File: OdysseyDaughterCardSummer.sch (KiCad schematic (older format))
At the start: 26 parts, among them J1 Conn_01x01, J2 Conn_01x01, J3 Conn_01x01, J4 Conn_01x01, X1 OdysseyDaughterCard

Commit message: R1.0 remove extra player hardware and replace with single port
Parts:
- removed D10, D9: 1N4448, Diode_THT:D_DO-35_SOD27_P7.62mm_Horizontal, symbol Device:D
- removed D11, D12: BAT83S, Diode_THT:D_DO-35_SOD27_P7.62mm_Horizontal, symbol Device:D_Schottky
- removed J1, J2, J3, J4: Conn_01x01, Connector_Wire:SolderWirePad_single_1-5mmDrill, symbol Connector_Generic:Conn_01x01
- removed R8, R9: 0, Resistor_THT:R_Axial_DIN0207_L6.3mm_D2.5mm_P7.62mm_Horizontal, symbol Device:R
- added J1: Conn_01x02, Connector_PinHeader_2.54mm:PinHeader_1x02_P2.54mm_Vertical, symbol Connector_Generic:Conn_01x02
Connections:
- wire segments 63 -> 50
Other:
- note added: "Ball Signal Out"
- note added: "Extra Players In"
- note removed: "Extra player inputs"
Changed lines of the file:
@@
 Sheet 1 1
 Title "Odyssey Daughter Card Summer"
-Date "2018-08-18"
-Rev "0.1"
+Date "2018-11-23"
+Rev "1.0"
 Comp "University of Pittsburgh - Odyssey Restoration Project"
 Comment1 "Levi Burner"
@@
 Card10
 $Comp
-L Device:D D10
-U 1 1 5B790856
-P 5750 3200
-F 0 "D10" H 5750 2984 50  0000 C CNN
-F 1 "1N4448" H 5750 3075 50  0000 C CNN
-F 2 "Diode_THT:D_DO-35_SOD27_P7.62mm_Horizontal" H 5750 3200 50  0001 C CNN
-F 3 "~" H 5750 3200 50  0001 C CNN
-	1    5750 3200
-	-1   0    0    1
-$EndComp
-$Comp
-L Device:D D9
-U 1 1 5B790898
-P 5750 2500
-F 0 "D9" H 5750 2284 50  0000 C CNN
-F 1 "1N4448" H 5750 2375 50  0000 C CNN
-F 2 "Diode_THT:D_DO-35_SOD27_P7.62mm_Horizontal" H 5750 2500 50  0001 C CNN
-F 3 "~" H 5750 2500 50  0001 C CNN
-	1    5750 2500
-	-1   0    0    1
-$EndComp
-Wire Wire Line
-	5900 3200 6000 3200
-Wire Wire Line
-	6000 3200 6000 3750
-Wire Wire Line
-	5900 2500 6000 2500
-Wire Wire Line
-	6000 2500 6000 3200
-Connection ~ 6000 3200
-Wire Wire Line
-	5600 2500 5550 2500
-Wire Wire Line
-	5600 3200 5550 3200
-$Comp
-L Connector_Generic:Conn_01x01 J3
-U 1 1 5B7939F4
-P 4550 3200
-F 0 "J3" H 4470 2975 50  0000 C CNN
-F 1 "Conn_01x01" H 4470 3066 50  0000 C CNN
-F 2 "Connector_Wire:SolderWirePad_single_1-5mmDrill" H 4550 3200 50  0001 C CNN
-F 3 "~" H 4550 3200 50  0001 C CNN
-	1    4550 3200
-	-1   0    0    1
-$EndComp
-$Comp
-L Connector_Generic:Conn_01x01 J1
-U 1 1 5B793A6A
-P 4550 2500
-F 0 "J1" H 4470 2275 50  0000 C CNN
-F 1 "Conn_01x01" H 4470 2366 50  0000 C CNN
-F 2 "Connector_Wire:SolderWirePad_single_1-5mmDrill" H 4550 2500 50  0001 C CNN
-F 3 "~" H 4550 2500 50  0001 C CNN
-	1    4550 2500
-	-1   0    0    1
-$EndComp
-$Comp
-L Device:R R8
-U 1 1 5B797289
-P 5400 2500
-F 0 "R8" V 5607 2500 50  0000 C CNN
-F 1 "0" V 5516 2500 50  0000 C CNN
-F 2 "Resistor_THT:R_Axial_DIN0207_L6.3mm_D2.5mm_P7.62mm_Horizontal" V 5330 2500 50  0001 C CNN
-F 3 "~" H 5400 2500 50  0001 C CNN
-	1    5400 2500
-	0    -1   -1   0
-$EndComp
-Wire Wire Line
-	5250 2500 5200 2500
-$Comp
-L Device:R R9
-U 1 1 5B797380
-P 5400 3200
-F 0 "R9" V 5607 3200 50  0000 C CNN
-F 1 "0" V 5516 3200 50  0000 C CNN
-F 2 "Resistor_THT:R_Axial_DIN0207_L6.3mm_D2.5mm_P7.62mm_Horizontal" V 5330 3200 50  0001 C CNN
-F 3 "~" H 5400 3200 50  0001 C CNN
-	1    5400 3200
-	0    -1   -1   0
-$EndComp
-Wire Wire Line
-	5250 3200 5200 3200
-$Comp
 L Device:R R4
 U 1 1 5B7991E8
@@
 	5250 5950 4750 5950
 $Comp
-L Device:D_Schottky D12
-U 1 1 5B7997A7
-P 5000 3550
-F 0 "D12" H 5000 3334 50  0000 C CNN
-F 1 "BAT83S" H 5000 3425 50  0000 C CNN
-F 2 "Diode_THT:D_DO-35_SOD27_P7.62mm_Horizontal" H 5000 3550 50  0001 C CNN
-F 3 "~" H 5000 3550 50  0001 C CNN
-	1    5000 3550
-	-1   0    0    1
-$EndComp
-$Comp
-L Device:D_Schottky D11
-U 1 1 5B79985B
-P 5000 2850
-F 0 "D11" H 5000 2634 50  0000 C CNN
-F 1 "BAT83S" H 5000 2725 50  0000 C CNN
-F 2 "Diode_THT:D_DO-35_SOD27_P7.62mm_Horizontal" H 5000 2850 50  0001 C CNN
-F 3 "~" H 5000 2850 50  0001 C CNN
-	1    5000 2850
-	-1   0    0    1
-$EndComp
-$Comp
-L Connector_Generic:Conn_01x01 J2
-U 1 1 5B79DE19
-P 4550 2850
-F 0 "J2" H 4470 2625 50  0000 C CNN
-F 1 "Conn_01x01" H 4470 2716 50  0000 C CNN
-F 2 "Connector_Wire:SolderWirePad_single_1-5mmDrill" H 4550 2850 50  0001 C CNN
-F 3 "~" H 4550 2850 50  0001 C CNN
-	1    4550 2850
-	-1   0    0    1
-$EndComp
-Wire Wire Line
-	4750 2850 4850 2850
-Wire Wire Line
-	5150 2850 5200 2850
-Wire Wire Line
-	5200 2850 5200 2500
-Connection ~ 5200 2500
-Wire Wire Line
-	5200 2500 4750 2500
-$Comp
-L Connector_Generic:Conn_01x01 J4
-U 1 1 5B7A2B6E
-P 4550 3550
-F 0 "J4" H 4470 3325 50  0000 C CNN
-F 1 "Conn_01x01" H 4470 3416 50  0000 C CNN
-F 2 "Connector_Wire:SolderWirePad_single_1-5mmDrill" H 4550 3550 50  0001 C CNN
-F 3 "~" H 4550 3550 50  0001 C CNN
-	1    4550 3550
-	-1   0    0    1
-$EndComp
-Wire Wire Line
-	5150 3550 5200 3550
-Wire Wire Line
-	5200 3550 5200 3200
-Connection ~ 5200 3200
-Wire Wire Line
-	5200 3200 4750 3200
-Wire Wire Line
-	4750 3550 4850 3550
-Wire Notes Line
-	4300 2200 4300 3650
-Wire Notes Line
-	4300 3650 5250 3650
-Wire Notes Line
-	5250 3650 5250 3400
-Wire Notes Line
-	5250 3400 6100 3400
-Wire Notes Line
-	6100 3400 6100 2200
-Wire Notes Line
-	6100 2200 4300 2200
-Text Notes 4300 2150 0    60   ~ 0
-Extra player inputs
+L Connector_Generic:Conn_01x02 J1
+U 1 1 5BF8D91F
+P 4800 2800
+F 0 "J1" H 4720 3017 50  0000 C CNN
+F 1 "Conn_01x02" H 4720 2926 50  0000 C CNN
+F 2 "Connector_PinHeader_2.54mm:PinHeader_1x02_P2.54mm_Vertical" H 4800 2800 50  0001 C CNN
+F 3 "~" H 4800 2800 50  0001 C CNN
+	1    4800 2800
+	-1   0    0    -1
+$EndComp
+Wire Wire Line
+	5000 2900 5200 2900
+Wire Wire Line
+	6000 2800 6000 3750
+Wire Wire Line
+	5000 2800 6000 2800
+Text Label 5200 2900 0    60   ~ 0
+Card5
+Text Notes 3950 2800 0    60   ~ 0
+Extra Players In
+Text Notes 3950 2900 0    60   ~ 0
+Ball Signal Out
 $EndSCHEMATC

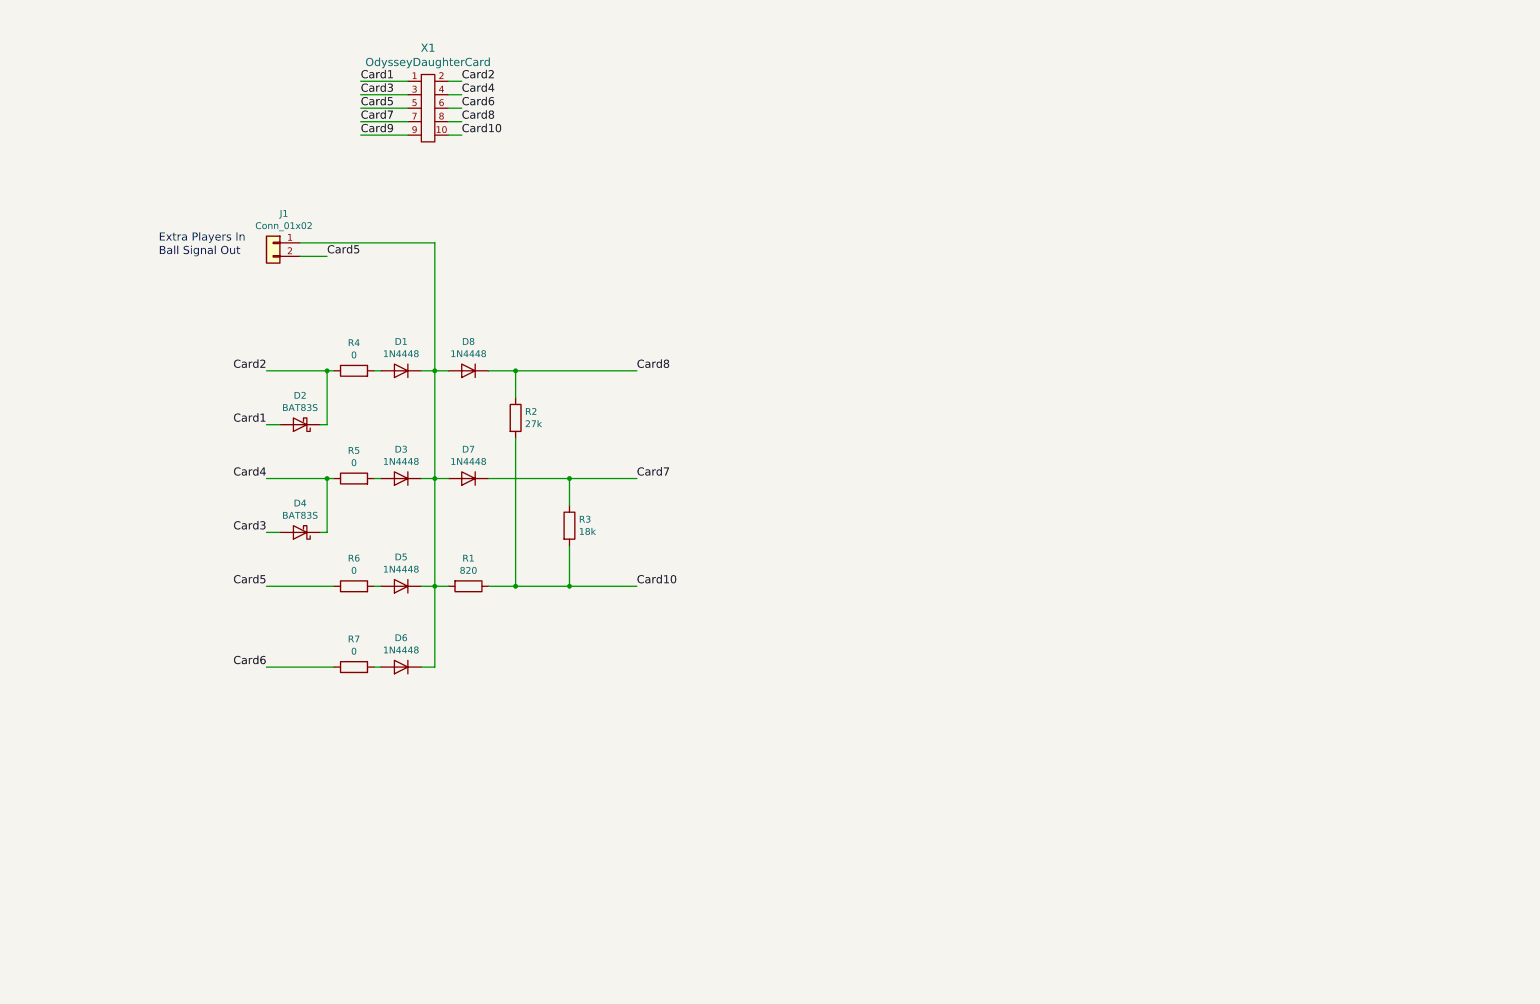
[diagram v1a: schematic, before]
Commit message: R1.1 with video mod pre layout
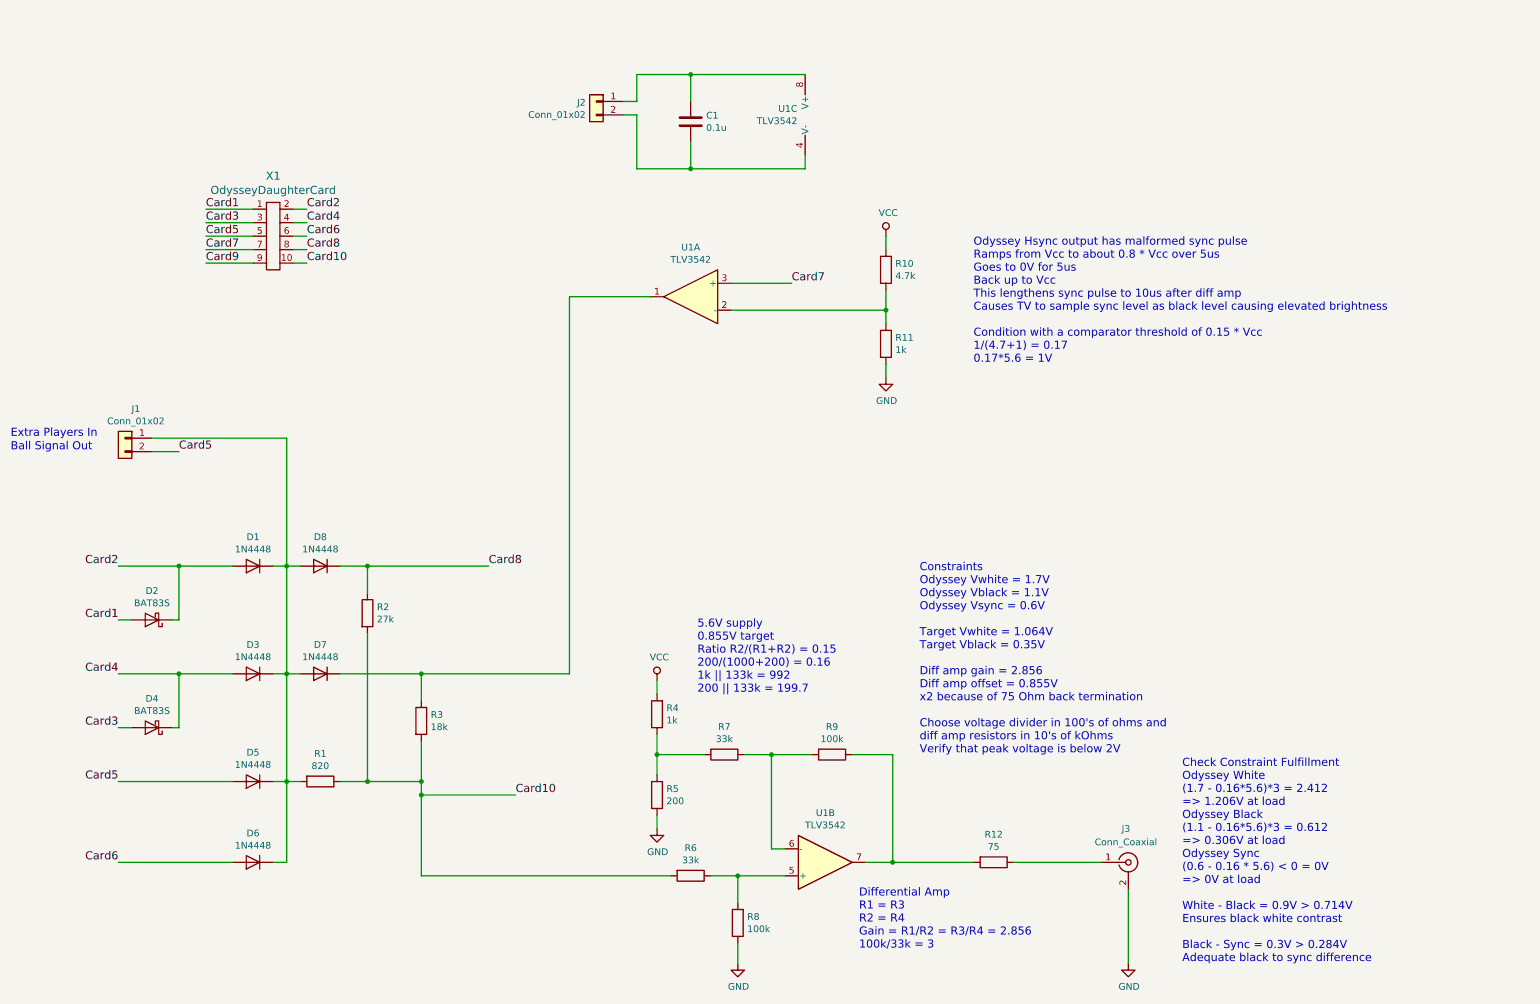
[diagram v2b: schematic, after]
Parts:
- added C1: 0.1u, Capacitor_THT:C_Disc_D3.8mm_W2.6mm_P2.50mm, symbol Device:C
- added J2: Conn_01x02, Connector_PinHeader_2.54mm:PinHeader_1x02_P2.54mm_Vertical, symbol Connector_Generic:Conn_01x02
- added J3: Conn_Coaxial, RCA_Switchcraft_PJRAN1X1U04X:CONN_RCA_JACK_MONO_3.2MM_Switchcraft_PJRAN1X1U04X, symbol Connector:Conn_Coaxial
- added R10: 4.7k, Resistor_THT:R_Axial_DIN0207_L6.3mm_D2.5mm_P7.62mm_Horizontal, symbol Device:R
- added R11: 1k, Resistor_THT:R_Axial_DIN0207_L6.3mm_D2.5mm_P7.62mm_Horizontal, symbol Device:R
- added R12: 75, Resistor_THT:R_Axial_DIN0207_L6.3mm_D2.5mm_P7.62mm_Horizontal, symbol Device:R
- added R8, R9: 100k, Resistor_THT:R_Axial_DIN0207_L6.3mm_D2.5mm_P7.62mm_Horizontal, symbol Device:R
- added U1: TLV3542, Package_SO:SOIC-8_3.9x4.9mm_P1.27mm, symbol TLV3542:TLV3542
- R4: value 0 -> 1k
- R5: value 0 -> 200
- R6, R7: value 0 -> 33k
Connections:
- net Card10: now also R6.2
- net Card2: now also D1.2 (A); no longer R4.1
- net Card4: now also D3.2 (A); no longer R5.1
- net Card5: now also D5.2 (A); no longer R6.1
- net Card6: now also D6.2 (A); no longer R7.1
- net Card7: now also U1.3 (+); no longer D7.1 (K), R3.1
- net VCC: now reaches R4.2
- net VCC: now also R10.1; no longer D1.2 (A)
- net at R5.2: now also R4.1, R7.2; no longer D3.2 (A)
- new net: D7.1 (K), R3.1, U1.1
- new net: R10.2, R11.1, U1.2 (-)
- new net: R6.1, R8.2, U1.5 (+)
- new net: R7.1, R9.2, U1.6 (-)
- new net: R12.2, R9.1, U1.7
- new net: C1.2, J2.2 (Pin_2), U1.4 (V-)
- new net: C1.1, J2.1 (Pin_1), U1.8 (V+)
- new net: J3.1 (In), R12.1
- new net GND: J3.2 (Ext), R11.2, R5.1, R8.1
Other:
- note added: "5.6V supply\n0.855V target\nRatio R2/(R1+R2) = 0.15\n200/(1000+200) = 0.16\n1k || 133k = 992\n200 || 133k = 199.7"
- note added: "Check Constraint Fulfillment\nOdyssey White\n(1.7 - 0.16*5.6)*3 = 2.412 \n=> 1.206V at load\nOdyssey Black\n(1.1 - 0.16*5.6)*3 = 0.612\n=> 0.306V at load\nOdyssey Sync\n(0.6 - 0.16 * 5.6) < 0 = 0V\n=> 0V at load\n\nWhite - Black = 0.9V > 0.714V\nEnsures black white contrast\n\nBlack - Sync = 0.3V > 0.284V\nAdequate black to sync difference"
- note added: "Constraints\nOdyssey Vwhite = 1.7V\nOdyssey Vblack = 1.1V\nOdyssey Vsync = 0.6V\n\nTarget Vwhite = 1.064V\nTarget Vblack = 0.35V\n\nDiff amp gain = 2.856\nDiff amp offset = 0.855V\nx2 because of 75 Ohm back termination\n\nChoose voltage divider in 100's of ohms and\ndiff amp resistors in 10's of kOhms\nVerify that peak voltage is below 2V"
- note added: "Differential Amp\nR1 = R3\nR2 = R4\nGain = R1/R2 = R3/R4 = 2.856\n100k/33k = 3"
- note added: "Odyssey Hsync output has malformed sync pulse\nRamps from Vcc to about 0.8 * Vcc over 5us\nGoes to 0V for 5us\nBack up to Vcc\nThis lengthens sync pulse to 10us after diff amp\nCauses TV to sample sync level as black level causing elevated brightness\n\nCondition with a comparator threshold of 0.15 * Vcc\n1/(4.7+1) = 0.17\n0.17*5.6 = 1V"
- moved on the sheet: D1, D2, D3, D4, D5, D6, D7, D8, J1, R1, R2, R3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

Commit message: R1.1 gerbs and board NTSC generator
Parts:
- J3: footprint RCA_Switchcraft_PJRAN1X1U04X:CONN_RCA_JACK_MONO_3.2MM_Switchcraft_PJRAN1X1U04X -> Connector_PinHeader_2.54mm:PinHeader_1x02_P2.54mm_Vertical
- R4: value 1k -> 4.7k
- R5: value 200 -> 820
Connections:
- net GND: now also C1.2, J2.2 (Pin_2), U1.4 (V-)
- net VCC: now also C1.1, J2.1 (Pin_1), U1.8 (V+)
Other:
- note added: "5.6V supply\n0.855V target\nRatio R2/(R1+R2) = 0.15\n820/(4700+820) = 0.15\n4.7k || 133k = 4.5k\n820 || 133k = 815"
- note added: "Check Constraint Fulfillment\nOdyssey White\n(1.7 - 0.15*5.6)*3 = 2.58 \n=> 1.29V at load\nOdyssey Black\n(1.1 - 0.16*5.6)*3 = 0.780\n=> 0.390V at load\nOdyssey Sync\n(0.6 - 0.15 * 5.6) < 0 = 0V\n=> 0V at load\n\nWhite - Black = 0.9V > 0.714V\nEnsures black white contrast\n\nBlack - Sync = 0.39V > 0.284V\nAdequate black to sync difference"
- note removed: "5.6V supply\n0.855V target\nRatio R2/(R1+R2) = 0.15\n200/(1000+200) = 0.16\n1k || 133k = 992\n200 || 133k = 199.7"
- note removed: "Check Constraint Fulfillment\nOdyssey White\n(1.7 - 0.16*5.6)*3 = 2.412 \n=> 1.206V at load\nOdyssey Black\n(1.1 - 0.16*5.6)*3 = 0.612\n=> 0.306V at load\nOdyssey Sync\n(0.6 - 0.16 * 5.6) < 0 = 0V\n=> 0V at load\n\nWhite - Black = 0.9V > 0.714V\nEnsures black white contrast\n\nBlack - Sync = 0.3V > 0.284V\nAdequate black to sync difference"
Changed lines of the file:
@@
 Wire Wire Line
 	4650 2850 4300 2850
-Wire Wire Line
-	4650 2950 4300 2950
 $Comp
 L Device:D D1
@@
 F 3 "" H 8750 1850 50  0001 C CNN
 	3    8750 1850
-	-1   0    0    -1
+	1    0    0    -1
 $EndComp
 $Comp
@@
 P 7650 6300
 F 0 "R4" H 7580 6254 50  0000 R CNN
-F 1 "1k" H 7580 6345 50  0000 R CNN
+F 1 "4.7k" H 7580 6345 50  0000 R CNN
 F 2 "Resistor_THT:R_Axial_DIN0207_L6.3mm_D2.5mm_P7.62mm_Horizontal" V 7580 6300 50  0001 C CNN
 F 3 "~" H 7650 6300 50  0001 C CNN
@@
 P 7650 6900
 F 0 "R5" H 7580 6854 50  0000 R CNN
-F 1 "200" H 7580 6945 50  0000 R CNN
+F 1 "820" H 7580 6945 50  0000 R CNN
 F 2 "Resistor_THT:R_Axial_DIN0207_L6.3mm_D2.5mm_P7.62mm_Horizontal" V 7580 6900 50  0001 C CNN
 F 3 "~" H 7650 6900 50  0001 C CNN
@@
 Wire Wire Line
 	9400 7400 10000 7400
-$Comp
-L Connector:Conn_Coaxial J3
-U 1 1 5C5FC8A0
-P 11150 7400
-F 0 "J3" H 11100 7650 50  0000 L CNN
-F 1 "Conn_Coaxial" H 10900 7550 50  0000 L CNN
-F 2 "RCA_Switchcraft_PJRAN1X1U04X:CONN_RCA_JACK_MONO_3.2MM_Switchcraft_PJRAN1X1U04X" H 11150 7400 50  0001 C CNN
-F 3 " ~" H 11150 7400 50  0001 C CNN
-	1    11150 7400
-	1    0    0    -1
-$EndComp
 Wire Wire Line
 	10300 7400 10950 7400
@@
 Constraints\nOdyssey Vwhite = 1.7V\nOdyssey Vblack = 1.1V\nOdyssey Vsync = 0.6V\n\nTarget Vwhite = 1.064V\nTarget Vblack = 0.35V\n\nDiff amp gain = 2.856\nDiff amp offset = 0.855V\nx2 because of 75 Ohm back termination\n\nChoose voltage divider in 100's of ohms and\ndiff amp resistors in 10's of kOhms\nVerify that peak voltage is below 2V
 Text Notes 7950 6150 0    60   ~ 0
-5.6V supply\n0.855V target\nRatio R2/(R1+R2) = 0.15\n200/(1000+200) = 0.16\n1k || 133k = 992\n200 || 133k = 199.7
+5.6V supply\n0.855V target\nRatio R2/(R1+R2) = 0.15\n820/(4700+820) = 0.15\n4.7k || 133k = 4.5k\n820 || 133k = 815
 Text Notes 9150 8050 0    60   ~ 0
 Differential Amp\nR1 = R3\nR2 = R4\nGain = R1/R2 = R3/R4 = 2.856\n100k/33k = 3
@@
 	5900 6000 7000 6000
 Text Notes 11550 8150 0    60   ~ 0
-Check Constraint Fulfillment\nOdyssey White\n(1.7 - 0.16*5.6)*3 = 2.412 \n=> 1.206V at load\nOdyssey Black\n(1.1 - 0.16*5.6)*3 = 0.612\n=> 0.306V at load\nOdyssey Sync\n(0.6 - 0.16 * 5.6) < 0 = 0V\n=> 0V at load\n\nWhite - Black = 0.9V > 0.714V\nEnsures black white contrast\n\nBlack - Sync = 0.3V > 0.284V\nAdequate black to sync difference
+Check Constraint Fulfillment\nOdyssey White\n(1.7 - 0.15*5.6)*3 = 2.58 \n=> 1.29V at load\nOdyssey Black\n(1.1 - 0.16*5.6)*3 = 0.780\n=> 0.390V at load\nOdyssey Sync\n(0.6 - 0.15 * 5.6) < 0 = 0V\n=> 0V at load\n\nWhite - Black = 0.9V > 0.714V\nEnsures black white contrast\n\nBlack - Sync = 0.39V > 0.284V\nAdequate black to sync difference
 $Comp
 L power:GND #PWR05
@@
 Text Notes 10000 3700 0    60   ~ 0
 Odyssey Hsync output has malformed sync pulse\nRamps from Vcc to about 0.8 * Vcc over 5us\nGoes to 0V for 5us\nBack up to Vcc\nThis lengthens sync pulse to 10us after diff amp\nCauses TV to sample sync level as black level causing elevated brightness\n\nCondition with a comparator threshold of 0.15 * Vcc\n1/(4.7+1) = 0.17\n0.17*5.6 = 1V
+$Comp
+L power:GND #PWR0101
+U 1 1 5C6326CE
+P 7500 2400
+F 0 "#PWR0101" H 7500 2150 50  0001 C CNN
+F 1 "GND" H 7505 2227 50  0000 C CNN
+F 2 "" H 7500 2400 50  0001 C CNN
+F 3 "" H 7500 2400 50  0001 C CNN
+	1    7500 2400
+	1    0    0    -1
+$EndComp
+Wire Wire Line
+	7500 2250 7500 2400
+Connection ~ 7500 2250
+$Comp
+L power:VCC #PWR0102
+U 1 1 5C634692
+P 7500 1300
+F 0 "#PWR0102" H 7500 1150 50  0001 C CNN
+F 1 "VCC" H 7517 1473 50  0000 C CNN
+F 2 "" H 7500 1300 50  0001 C CNN
+F 3 "" H 7500 1300 50  0001 C CNN
+	1    7500 1300
+	1    0    0    -1
+$EndComp
+Wire Wire Line
+	7500 1300 7500 1550
+Connection ~ 7500 1550
+Wire Wire Line
+	4650 2950 4300 2950
+$Comp
+L Connector:Conn_Coaxial J3
+U 1 1 5C5FC8A0
+P 11150 7400
+F 0 "J3" H 11100 7650 50  0000 L CNN
+F 1 "Conn_Coaxial" H 10900 7550 50  0000 L CNN
+F 2 "Connector_PinHeader_2.54mm:PinHeader_1x02_P2.54mm_Vertical" H 11150 7400 50  0001 C CNN
+F 3 " ~" H 11150 7400 50  0001 C CNN
+	1    11150 7400
+	1    0    0    -1
+$EndComp
 $EndSCHEMATC

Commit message: Matt added pad to expansion header on 05-22-20
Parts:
- removed J1: Conn_01x02, Connector_PinHeader_2.54mm:PinHeader_1x02_P2.54mm_Vertical, symbol Connector_Generic:Conn_01x02
- added J1: Conn_01x03, Connector_PinHeader_2.54mm:PinHeader_1x03_P2.54mm_Vertical, symbol Connector_Generic:Conn_01x03
- X1: symbol Odyssey_Daughter_Card:OdysseyDaughterCard -> OdysseyDaughterCardSummer-rescue:OdysseyDaughterCard-Odyssey_Daughter_Card
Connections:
- wire segments 89 -> 91
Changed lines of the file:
@@
 $EndDescr
 $Comp
-L Odyssey_Daughter_Card:OdysseyDaughterCard X1
+L OdysseyDaughterCardSummer-rescue:OdysseyDaughterCard-Odyssey_Daughter_Card X1
 U 1 1 5B0D981F
 P 4800 2750
@@
 Text Label 6600 6900 0    60   ~ 0
 Card10
-$Comp
-L Connector_Generic:Conn_01x02 J1
-U 1 1 5BF8D91F
-P 3700 4250
-F 0 "J1" H 3620 4467 50  0000 C CNN
-F 1 "Conn_01x02" H 3620 4376 50  0000 C CNN
-F 2 "Connector_PinHeader_2.54mm:PinHeader_1x02_P2.54mm_Vertical" H 3700 4250 50  0001 C CNN
-F 3 "~" H 3700 4250 50  0001 C CNN
-	1    3700 4250
-	-1   0    0    -1
-$EndComp
 Wire Wire Line
 	3900 4350 4100 4350
@@
 Text Label 4100 4350 0    60   ~ 0
 Card5
-Text Notes 2850 4250 0    60   ~ 0
+Text Notes 2850 4210 0    60   ~ 0
 Extra Players In
 Text Notes 2850 4350 0    60   ~ 0
@@
 	1    0    0    -1
 $EndComp
+$Comp
+L Connector_Generic:Conn_01x03 J1
+U 1 1 5EC83BF2
+P 3700 4250
+F 0 "J1" H 3620 4567 50  0000 C CNN
+F 1 "Conn_01x03" H 3620 4476 50  0000 C CNN
+F 2 "Connector_PinHeader_2.54mm:PinHeader_1x03_P2.54mm_Vertical" H 3700 4250 50  0001 C CNN
+F 3 "~" H 3700 4250 50  0001 C CNN
+	1    3700 4250
+	-1   0    0    -1
+$EndComp
+Wire Wire Line
+	3900 4150 4900 4150
+Wire Wire Line
+	4900 4150 4900 4250
+Connection ~ 4900 4250
 $EndSCHEMATC
